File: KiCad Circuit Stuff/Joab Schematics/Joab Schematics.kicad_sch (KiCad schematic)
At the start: 46 parts, among them J1 Conn_02x16_Odd_Even, J2 Conn_01x02, Q1 MMBT3904, Q2 S8550, U1 MT3608, U2 AMS1117-3.3, U3 MCP73831-2-OT, U5 TPS5430DDA

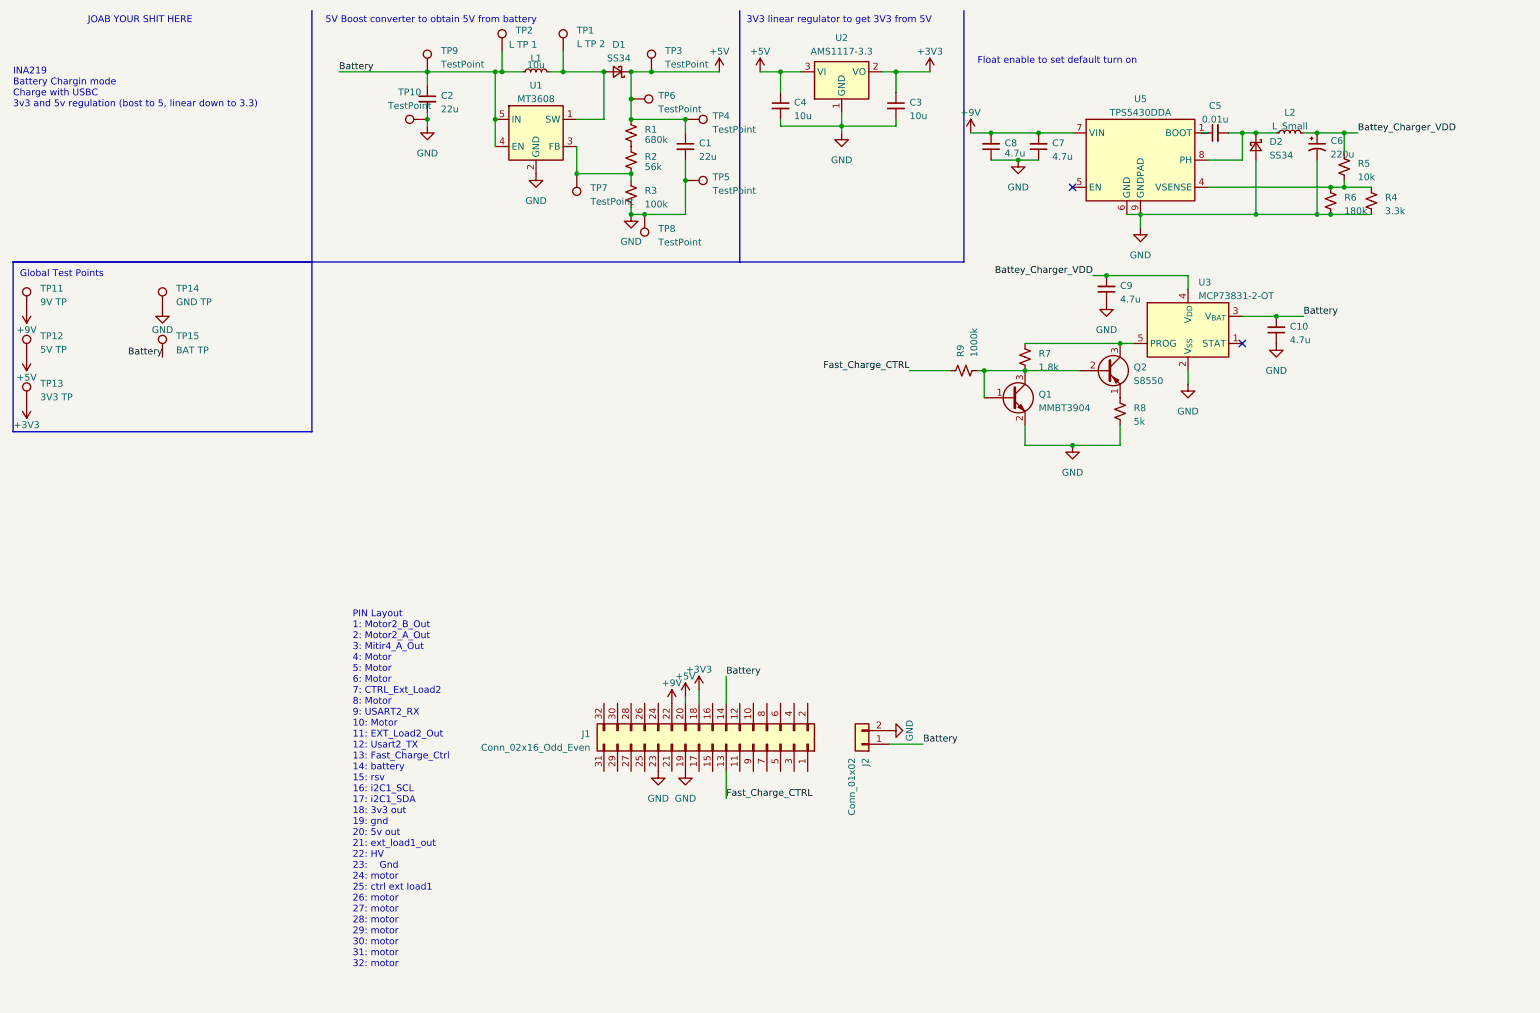
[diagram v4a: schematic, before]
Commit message: Added INA219 monitor (kinda) and added some fixes
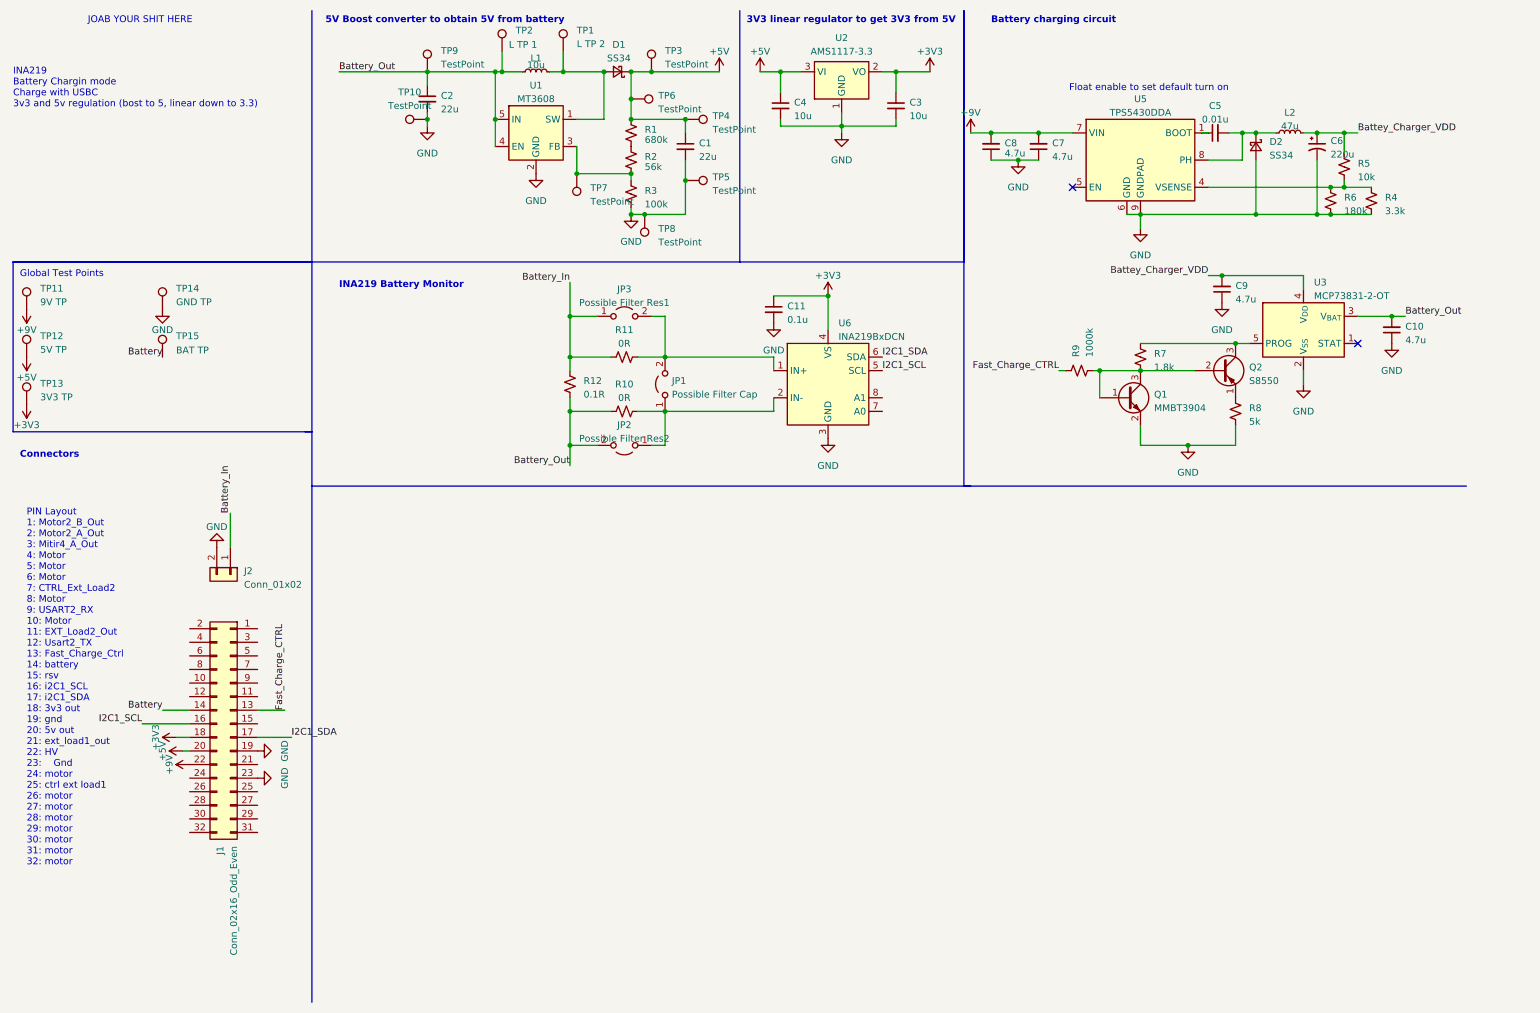
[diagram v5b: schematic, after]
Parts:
- added C11: 0.1u, Capacitor_SMD:C_0402_1005Metric_Pad0.74x0.62mm_HandSolder, symbol Device:C_Small
- added JP1: Possible Filter Cap, Jumper:SolderJumper-2_P1.3mm_Open_Pad1.0x1.5mm, symbol Jumper:Jumper_2_Open
- added JP2: Possible Filter Res2, Jumper:SolderJumper-2_P1.3mm_Open_Pad1.0x1.5mm, symbol Jumper:Jumper_2_Open
- added JP3: Possible Filter Res1, Jumper:SolderJumper-2_P1.3mm_Open_Pad1.0x1.5mm, symbol Jumper:Jumper_2_Open
- added R10, R11: 0R, Resistor_SMD:R_0402_1005Metric_Pad0.72x0.64mm_HandSolder, symbol Device:R_Small_US
- added R12: 0.1R, Resistor_SMD:R_0402_1005Metric_Pad0.72x0.64mm_HandSolder, symbol Device:R_Small_US
- added U6: INA219BxDCN, Package_TO_SOT_SMD:SOT-23-8, symbol Sensor_Energy:INA219BxDCN
- J1: footprint (none) -> Connector_PinHeader_2.54mm:PinHeader_2x16_P2.54mm_Vertical
- J2: footprint (none) -> Connector_JST:JST_PH_B2B-PH-K_1x02_P2.00mm_Vertical
- L1: footprint Inductor_SMD:L_0402_1005Metric_Pad0.77x0.64mm_HandSolder -> Inductor_SMD:L_Changjiang_FNR4030S; LCSC C9182 -> C167879
- L2: value L_Small -> 47u; footprint Inductor_SMD:L_0402_1005Metric_Pad0.77x0.64mm_HandSolder -> Inductor_SMD:L_Sunlord_SWPA5040S; LCSC C475913 -> C86617
- Q2: footprint Package_TO_SOT_THT:TO-92_Inline -> Package_TO_SOT_SMD:SOT-23
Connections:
- net +3V3: now also C11.1, U6.4 (VS)
- net Battery: no longer C10.2, C2.1, J2.1 (Pin_1), L1.1, TP2.1, TP9.1, U1.4 (EN), U1.5 (IN), U3.3 (V_{BAT})
- net GND: now also C11.2, U6.3 (GND)
- net I2C1_SCL: now reaches J1.16 (Pin_16)
- net I2C1_SCL: now also U6.5 (SCL)
- net I2C1_SDA: now reaches J1.17 (Pin_17)
- net I2C1_SDA: now also U6.6 (SDA)
- new net: JP1.2 (B), JP3.2 (B), R11.2, U6.1 (IN+)
- new net: JP1.1 (A), JP2.1 (A), R10.2, U6.2 (IN-)
- new net Battery_In: J2.1 (Pin_1), JP3.1 (A), R11.1, R12.2
- new net Battery_Out: C10.2, C2.1, JP2.2 (B), L1.1, R10.1, R12.1, TP2.1, TP9.1, U1.4 (EN), U1.5 (IN), U3.3 (V_{BAT})
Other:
- note added: "Battery charging circuit"
- note added: "Connectors"
- note added: "INA219 Battery Monitor"
- moved on the sheet: C10, C9, J1, J2, Q1, Q2, R7, R8, R9, U3

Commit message: Chaned Charrging IC, Chaned INA219 IC, Changed some other things
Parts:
- removed D1, D2: SS34, Diode_SMD:D_SMA_Handsoldering, symbol Device:D_Schottky_Small
- removed U3: MCP73831-2-OT, Package_TO_SOT_SMD:SOT-23-5, symbol Battery_Management:MCP73831-2-OT
- removed U6: INA219BxDCN, Package_TO_SOT_SMD:SOT-23-8, symbol Sensor_Energy:INA219BxDCN
- added D1, D2: SS34_C8678, JLCPCB:SMA_L4.3-W2.6-LS5.2-RD, symbol JLC-SS34:SS34_C8678
- added U3: TP4056, JLCPCB:ESOP-8_L4.9-W3.9-P1.27-LS6.0-BL-EP, symbol TP4056:TP4056
- added U4: INA219AIDCNR, JLCPCB:SOT-23-8_L3.0-W1.7-P0.65-LS2.8-BR, symbol JLC-INA219AIDCNR:INA219AIDCNR
- C10, C9: value 4.7u -> 10u
- R7: value 1.8k -> 2k
- R8: value 5k -> 5.5k
- TP1, TP10, TP11, TP12, TP13, TP14, TP15, TP2, TP3, TP4, TP5, TP6, TP7, TP8, TP9: footprint TestPoint:TestPoint_2Pads_Pitch2.54mm_Drill0.8mm -> TestPoint:TestPoint_Pad_2.5x2.5mm
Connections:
- net +3V3: now also U4.4 (VS), U4.8 (A1)
- net +5V: now also D1.1 (K); no longer C1.1, TP4.1
- net Battery_Out: now also U3.5 (BAT)
- net Battey_Charger_VDD: now also U3.4 (VCC), U3.8 (CE)
- net GND: now also D2.2 (A), U3.1 (TEMP), U3.3 (GND), U3.6 (STDBY#), U3.7 (CHRG#), U3.9 (EP), U4.3 (GND), U4.7 (A0)
- net I2C1_SCL: now also U4.5 (SCL)
- net I2C1_SDA: now also U4.6 (SDA)
- net at JP1.2 (B), JP3.2 (B), R11.2: now also U4.1 (IN+)
- net at JP1.1 (A), JP2.1 (A), R10.2: now also U4.2 (IN-)
- net at Q2.3 (C), R7.1: now also U3.2 (PROG)
- net at L1.2, TP1.1, U1.1 (SW): now also D1.2 (A)
- net at C5.2, L2.1, U5.8 (PH): now also D2.1 (K)
- new net: C1.1, TP4.1
- no-connect marks 2 -> 1
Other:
- note added: "CHANGE THESE RESISTORS"
- moved on the sheet: Q1, Q2, R7, R8, R9, TP3, TP6

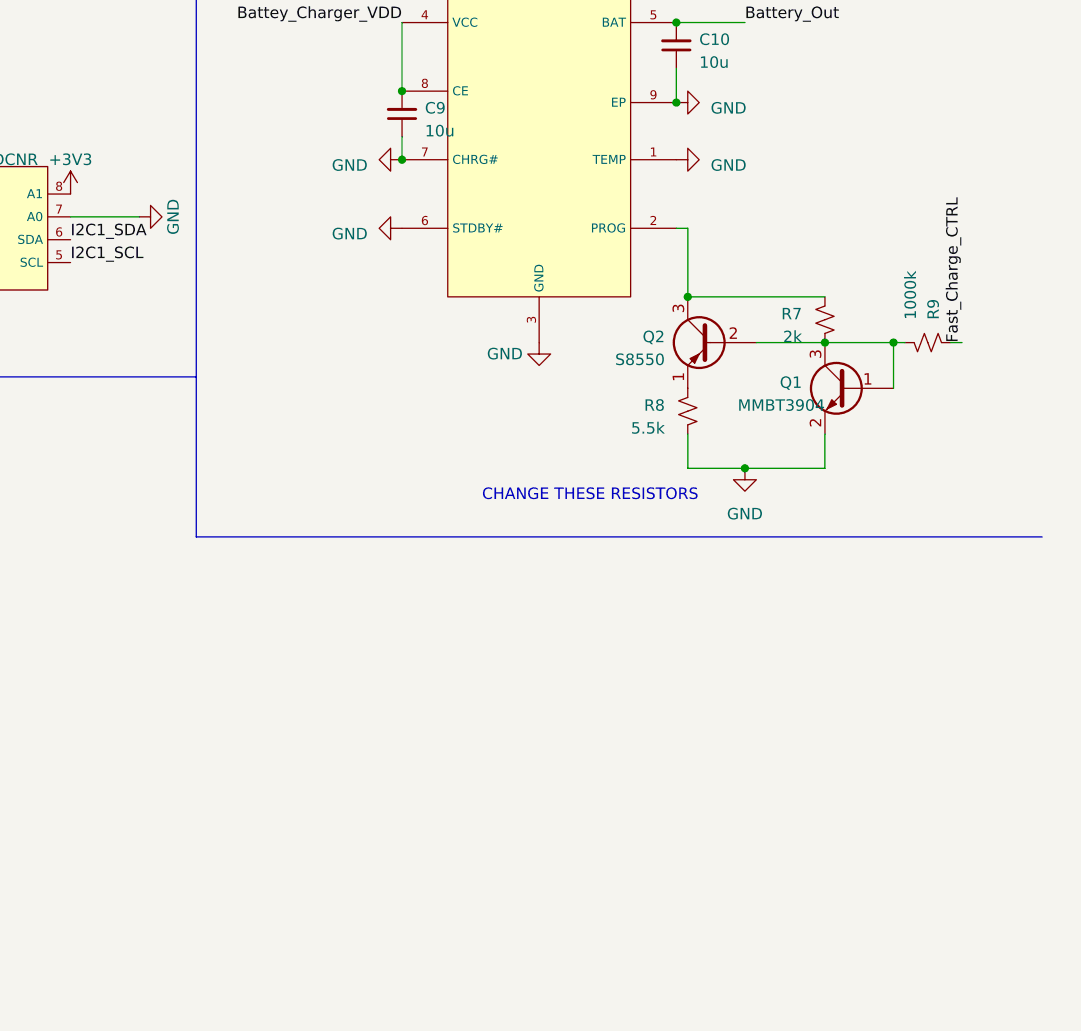
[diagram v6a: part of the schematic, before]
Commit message: Added Switching for charger
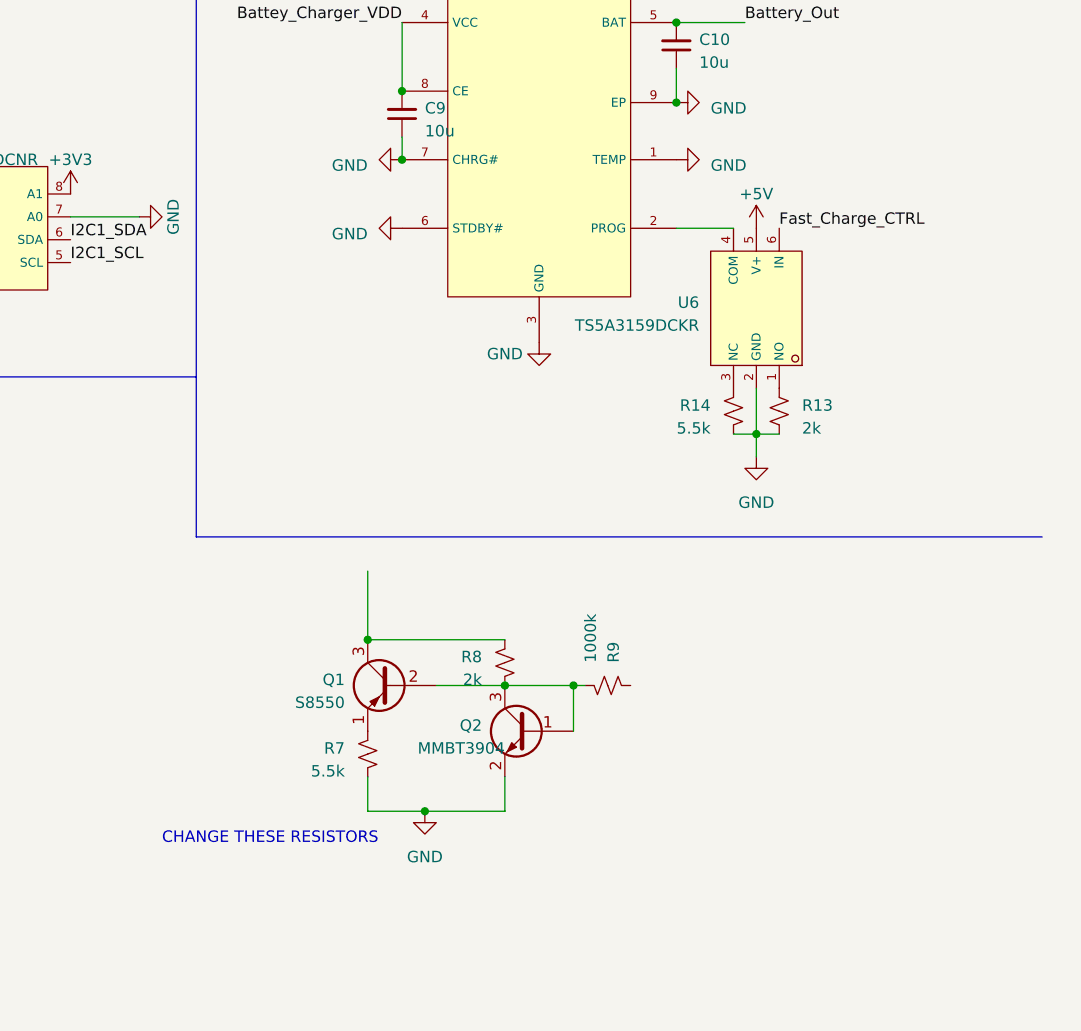
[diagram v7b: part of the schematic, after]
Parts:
- removed Q1: MMBT3904, Package_TO_SOT_SMD:SOT-23, symbol Transistor_BJT:MMBT3904
- removed Q2: S8550, Package_TO_SOT_SMD:SOT-23, symbol Transistor_BJT:S8550
- added Q1: S8550, Package_TO_SOT_SMD:SOT-23, symbol Transistor_BJT:S8550
- added Q2: MMBT3904, Package_TO_SOT_SMD:SOT-23, symbol Transistor_BJT:MMBT3904
- added R13: 2k, Resistor_SMD:R_0402_1005Metric_Pad0.72x0.64mm_HandSolder, symbol Device:R_Small_US
- added R14: 5.5k, Resistor_SMD:R_0402_1005Metric_Pad0.72x0.64mm_HandSolder, symbol Device:R_Small_US
- added U6: TS5A3159DCKR, JLCPCB:SC-70-6_L2.0-W1.3-P0.65-LS2.1-BL-1, symbol JLC-TS5A3159DCKR:TS5A3159DCKR
- R7: value 2k -> 5.5k
- R8: value 5.5k -> 2k
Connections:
- net +5V: now also U6.5 (V+)
- net Fast_Charge_CTRL: now also U6.6 (IN); no longer R9.1
- net GND: now also R7.2, Q2.2 (E), R13.2, R14.2, U6.2 (GND); no longer R8.2
- net at R7.1: now also Q1.1 (E); no longer U3.2 (PROG)
- net at R8.1: now also Q1.3 (C)
- net at R9.2: now also R8.2, Q1.2 (B), Q2.1 (B), Q2.3 (C); no longer R7.2
- new net: U3.2 (PROG), U6.4 (COM)
- new net: R13.1, U6.1 (NO)
- new net: R14.1, U6.3 (NC)

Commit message: Changed some values of resistors, caps and inductors, Also modified some components Still need to finish adding resistors from jlcpcb
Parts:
- removed C10, C3: 10u, Capacitor_SMD:C_0402_1005Metric_Pad0.74x0.62mm_HandSolder, symbol Device:C_Small
- removed C7: 4.7u, Capacitor_SMD:C_0402_1005Metric_Pad0.74x0.62mm_HandSolder, symbol Device:C_Small
- removed U5: TPS5430DDA, Package_SO:TI_SO-PowerPAD-8_ThermalVias, symbol Regulator_Switching:TPS5430DDA
- added C13: TAJA106K016RNJ, JLCPCB:CAP-SMD_L3.2-W1.6-RD-C7171, symbol JLC-TAJA106K016RNJ:TAJA106K016RNJ
- added C7: CA45-A-10V-22UF-K, JLCPCB:CASE-A_3216, symbol JLC-CA45-A-10V-22uF-K:CA45-A-10V-22UF-K
- added R15: 1.5R, Resistor_SMD:R_0402_1005Metric_Pad0.72x0.64mm_HandSolder, symbol Device:R_Small_US
- added U7: TPS5430DDAR, JLCPCB:ESOP-8_L4.9-W3.9-P1.27-LS6.0-TL-EP, symbol JLC-TPS5430DDAR:TPS5430DDAR
- C1: footprint Capacitor_SMD:C_0402_1005Metric_Pad0.74x0.62mm_HandSolder -> Capacitor_SMD:C_1206_3216Metric_Pad1.33x1.80mm_HandSolder; LCSC (none) -> C12891
- C11: value 0.1u -> 100p; footprint Capacitor_SMD:C_0402_1005Metric_Pad0.74x0.62mm_HandSolder -> Capacitor_SMD:C_0603_1608Metric_Pad1.08x0.95mm_HandSolder; LCSC (none) -> C14858
- C2: value 22u -> 10u; footprint Capacitor_SMD:C_0402_1005Metric_Pad0.74x0.62mm_HandSolder -> Capacitor_SMD:C_0603_1608Metric_Pad1.08x0.95mm_HandSolder; LCSC (none) -> C19702
- C4: value 10u -> 22u; footprint Capacitor_SMD:C_0402_1005Metric_Pad0.74x0.62mm_HandSolder -> Capacitor_SMD:C_1206_3216Metric_Pad1.33x1.80mm_HandSolder; LCSC (none) -> C12891
- C5: value 0.01u -> 10p; footprint Capacitor_SMD:C_0402_1005Metric_Pad0.74x0.62mm_HandSolder -> Capacitor_SMD:C_0603_1608Metric_Pad1.08x0.95mm_HandSolder; LCSC (none) -> C1634
- C6: footprint Capacitor_SMD:C_0402_1005Metric_Pad0.74x0.62mm_HandSolder -> Capacitor_SMD:C_Elec_6.3x7.7; LCSC (none) -> C19100600
- C8: footprint Capacitor_SMD:C_0402_1005Metric_Pad0.74x0.62mm_HandSolder -> Capacitor_SMD:C_0603_1608Metric_Pad1.08x0.95mm_HandSolder; LCSC (none) -> C19666
- C9: footprint Capacitor_SMD:C_0402_1005Metric_Pad0.74x0.62mm_HandSolder -> Capacitor_SMD:C_0603_1608Metric_Pad1.08x0.95mm_HandSolder; LCSC (none) -> C19702
- L2: value 47u -> 18u; footprint Inductor_SMD:L_Sunlord_SWPA5040S -> Inductor_SMD:L_Changjiang_FNR4030S; LCSC C86617 -> C167882
- R1: value 680k -> 220k; footprint Resistor_SMD:R_0402_1005Metric_Pad0.72x0.64mm_HandSolder -> Resistor_SMD:R_0603_1608Metric_Pad0.98x0.95mm_HandSolder; LCSC (none) -> C22961
- R2: value 56k -> 22k; footprint Resistor_SMD:R_0402_1005Metric_Pad0.72x0.64mm_HandSolder -> Resistor_SMD:R_0603_1608Metric_Pad0.98x0.95mm_HandSolder; LCSC (none) -> C31850
- R3: value 100k -> 33k; LCSC (none) -> C25779
- R4: value 3.3k -> 2.2k; LCSC (none) -> C25879
- R5: LCSC (none) -> C25744
- R6: value 180k -> 1k; LCSC (none) -> C11702
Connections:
- net +3V3: now also C7.1
- net +5V: now also C1.1, TP4.1, C13.1; no longer C4.1
- net +9V: now also U7.7 (VIN)
- net Battery_Out: now also C2.2, C4.1; no longer C2.1
- net GND: now also C2.1, R6.1, C13.2, C7.2, R15.2, U7.6 (GND), U7.9 (PowerPAD); no longer C2.2, C9.1, R4.2, R6.2
- net PH_Pin: now reaches C5.2, D2.1 (K), L2.1
- net PH_Pin: now also U7.8 (PH)
- net at C5.1: now also U7.1 (BOOT)
- net at R4.1, R5.2: now also U7.4 (VSENSE); no longer R6.1
- new net: C9.1, R15.1
- new net: R4.2, R6.2
- no-connect marks 1 -> 3
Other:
- note added: "Cange this resistor"
- note added: "RESISTORS FROM U3-> INA"
- moved on the sheet: C8, C9, R4, R5
